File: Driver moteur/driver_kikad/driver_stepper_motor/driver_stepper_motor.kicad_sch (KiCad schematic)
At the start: 10 parts, among them Con1 OutMot, Con2 Conn_01x04, U1 STM32G031G8U6

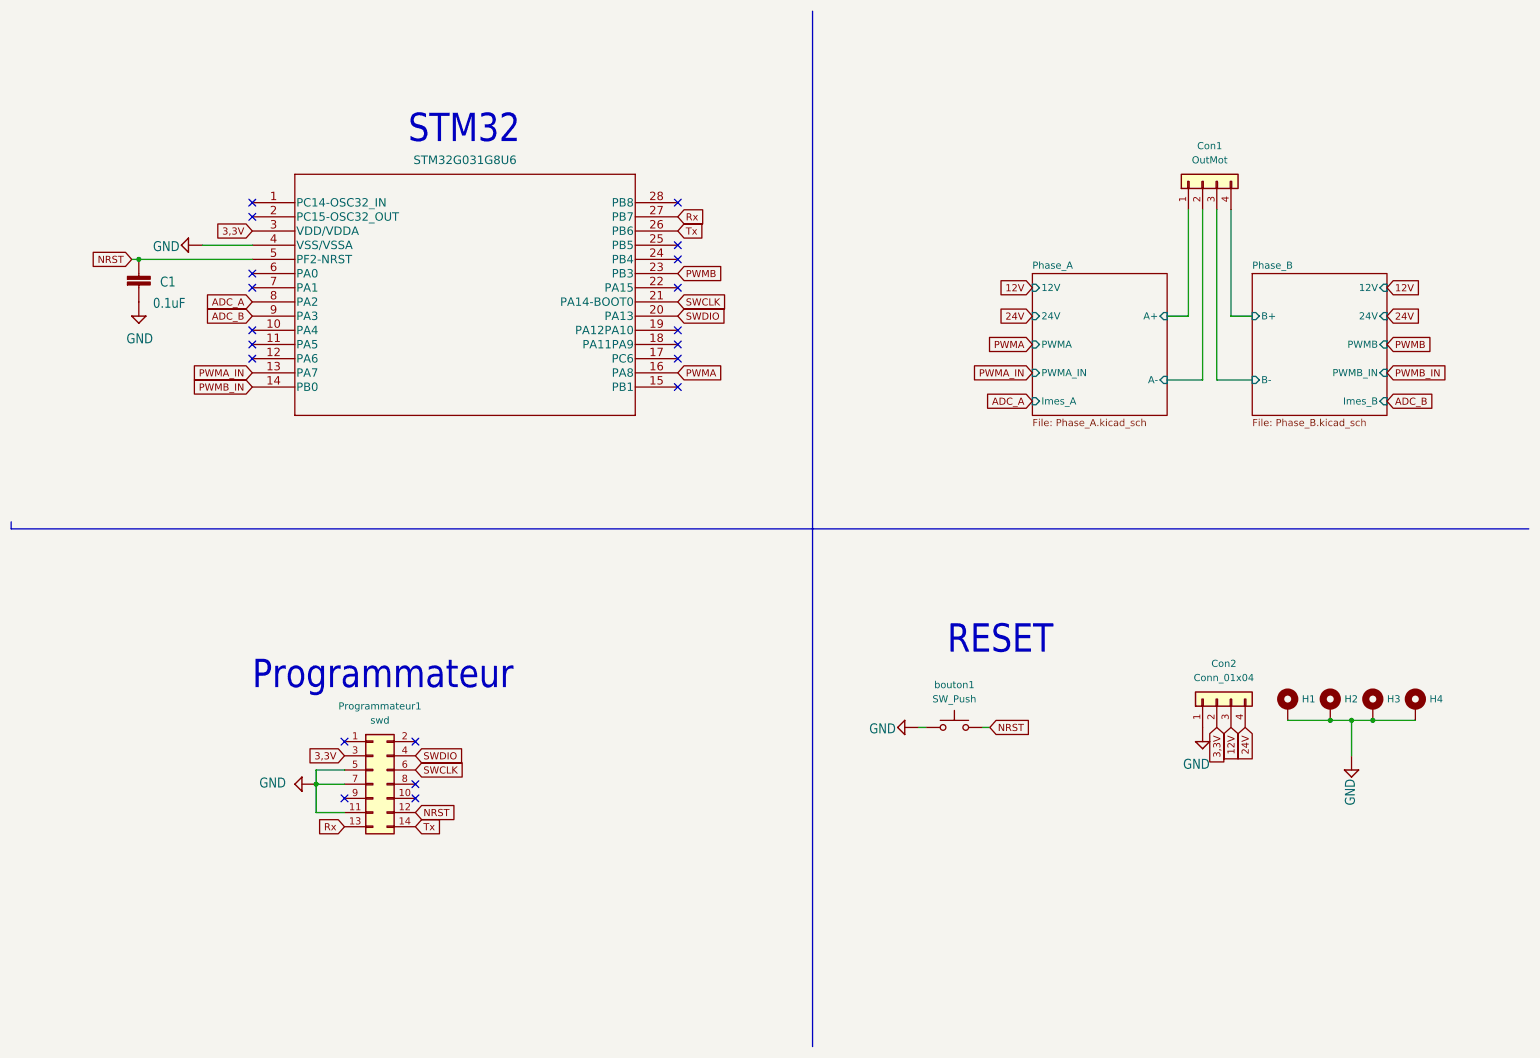
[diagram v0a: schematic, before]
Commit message: Driver modifié avec les bonnes valeurs et les bonnes datasheet
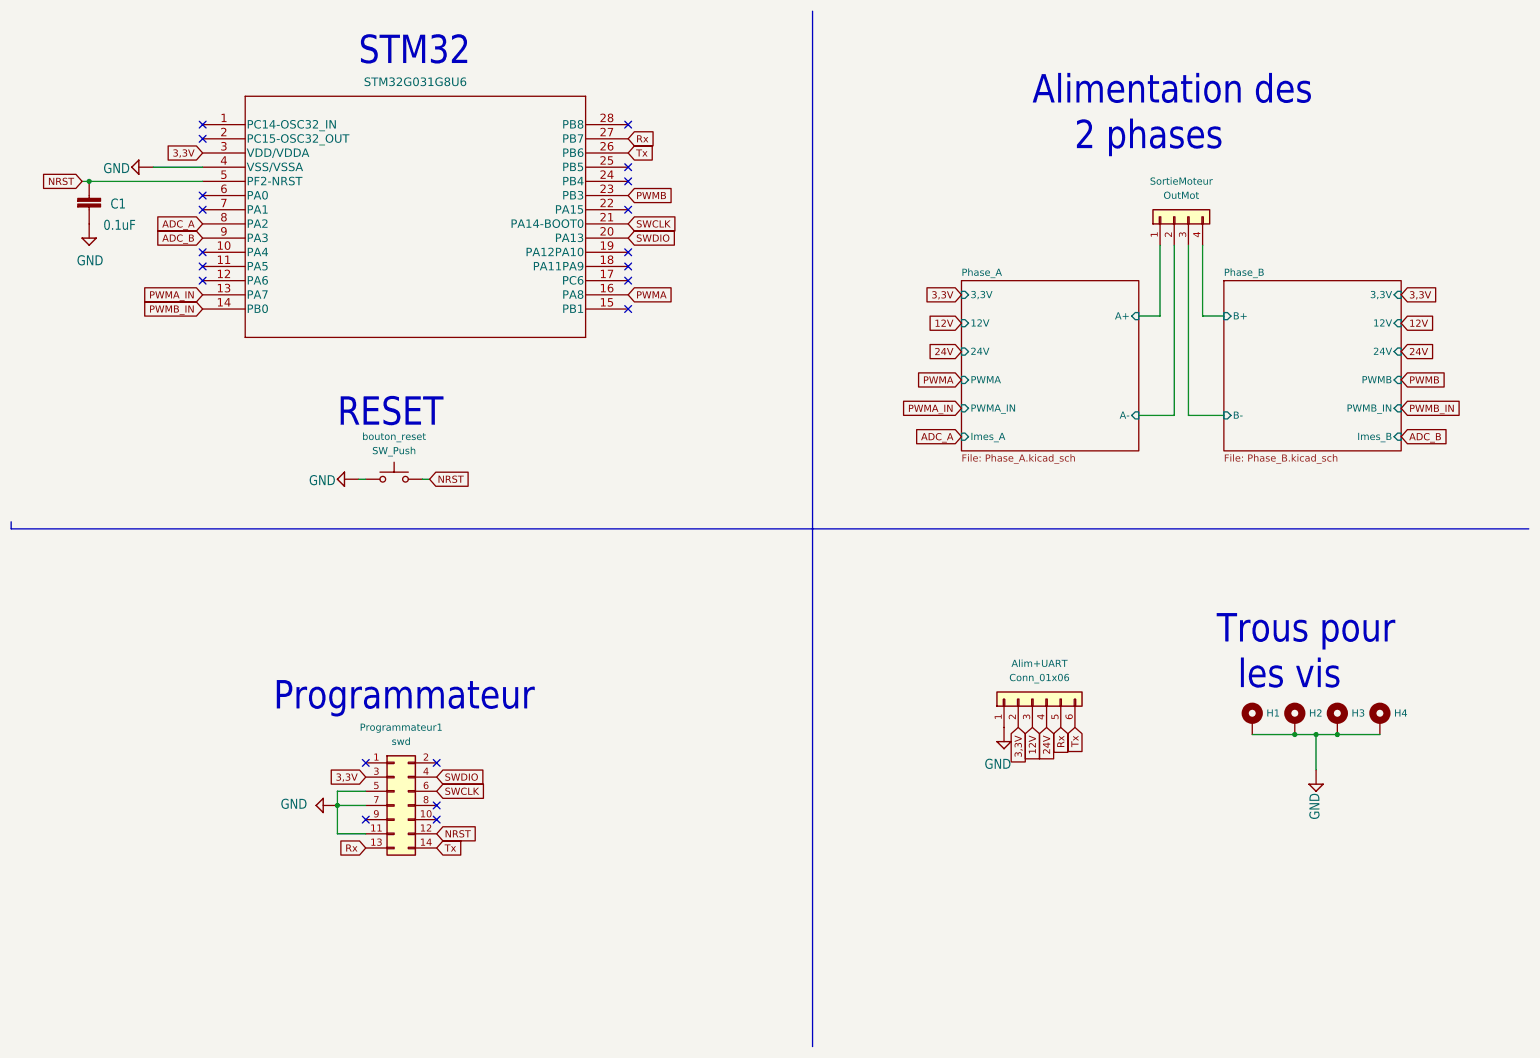
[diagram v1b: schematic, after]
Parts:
- removed Con2: Conn_01x04, Connector_JST:JST_XH_B4B-XH-A_1x04_P2.50mm_Vertical, symbol Connector_Generic:Conn_01x04
- added Alim+UART: Conn_01x06, symbol Connector_Generic:Conn_01x06
- renumbered Con1 to SortieMoteur, bouton1 to bouton_reset
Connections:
- net 12V: now also Alim+UART.3 (Pin_3)
- net 24V: now also Alim+UART.4 (Pin_4)
- net 3,3V: now also Alim+UART.2 (Pin_2)
- net GND: now also Alim+UART.1 (Pin_1)
- net Rx: now also Alim+UART.5 (Pin_5)
- net Tx: now also Alim+UART.6 (Pin_6)
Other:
- sheet Phase_A ports: added 3,3V; removed none
- sheet Phase_B ports: added 3,3V; removed none
- note added: "Alimentation des 2 phases"
- note added: "Trous pour les vis"
- moved on the sheet: C1, H1, H2, H3, H4, Programmateur1, SortieMoteur, bouton_reset

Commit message: PCB root sans erreurs
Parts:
- Alim+UART1: renamed from Alim+UART; footprint (none) -> Connector_JST:JST_XH_B6B-XH-A_1x06_P2.50mm_Vertical
- renumbered SortieMoteur to SortieMoteur1, bouton_reset to bouton_reset1
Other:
- moved on the sheet: SortieMoteur1

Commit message: modif push button
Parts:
- bouton_reset1: footprint Button_Switch_THT:SW_PUSH_6mm -> 2-1437565-7:SW_2-1437565-7
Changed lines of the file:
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@@
     (property "Reference" "bouton_reset1" (id 0) (at 81.28 88.9 0))
     (property "Value" "SW_Push" (id 1) (at 81.28 91.44 0))
-    (property "Footprint" "Button_Switch_THT:SW_PUSH_6mm" (id 2) (at 81.28 91.44 0)
+    (property "Footprint" "2-1437565-7:SW_2-1437565-7" (id 2) (at 81.28 91.44 0)
       (effects (font (size 1.27 1.27)) hide)
     )
@@
     )
     (path "/2c828bfa-0e4c-4f43-83ad-e7dc709243ae"
-      (reference "bouton_reset1") (unit 1) (value "SW_Push") (footprint "Button_Switch_THT:SW_PUSH_6mm")
-    )
-  )
+      (reference "bouton_reset1") (unit 1) (value "SW_Push") (footprint "2-1437565-7:SW_2-1437565-7")
+    )
+  )
